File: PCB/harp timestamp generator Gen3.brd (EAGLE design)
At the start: 124.5 x 80.4 mm, 140 parts, among them IC1 MCP73831T-2ATI/OT, IC10 SN74LVC1G125DBVT, IC11 TLV70033DDCR, IC12 SI8621BC-B-IS, IC13 SI8621BC-B-IS, IC14 SI8621BC-B-IS, IC15 SI8621BC-B-IS, IC16 SI8621BC-B-IS, IC17 SI8621BC-B-IS, IC18 SN74LVC1G125DBVT, IC19 SN74LVC1G125DBVT, IC2 USBLC6-2SC6, IC3 FT232RL, IC4 ICL7673CBAZA-T, IC5 TLV70033DDCR, IC6 ATXMEGA16A4U-AU, IC7 M74VHC1GT126DF1G, IC8 M74VHC1GT126DF1G, IC9 M74VHC1GT126DF1G, Q1 RTU002P02T106, Q2 BC817-40W, Q3 BC817-40LT1SMD, Q4 DMG1012UW, Q5 DMP2035U-7, T1 BC850, T10 BC850, T2 BC850, T3 BC850, T4 BC850, T5 BC850, T6 BC850, T7 BC850, T8 BC850, T9 BC850, X1 B2B-PH-K-S(LF)(SN)

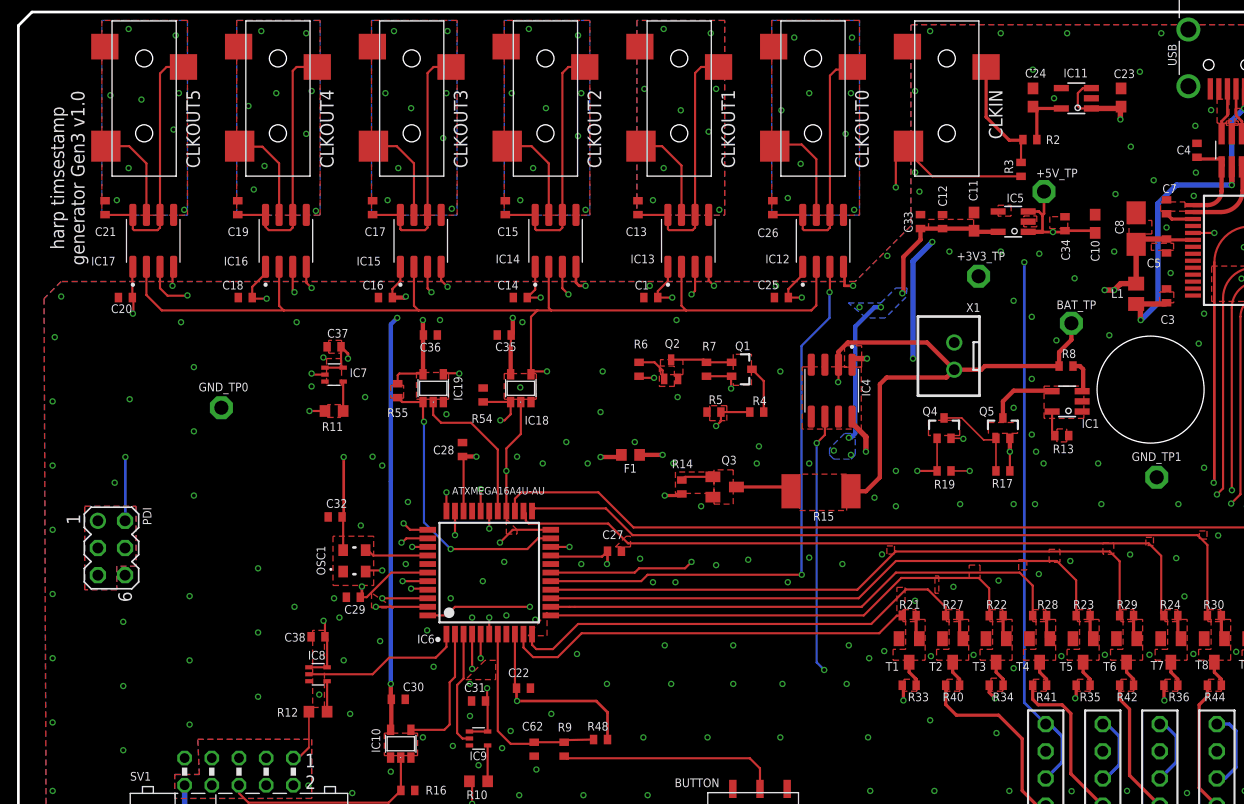
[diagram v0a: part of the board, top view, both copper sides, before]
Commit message: Added an extra 100uF capacitor to +5_USB.
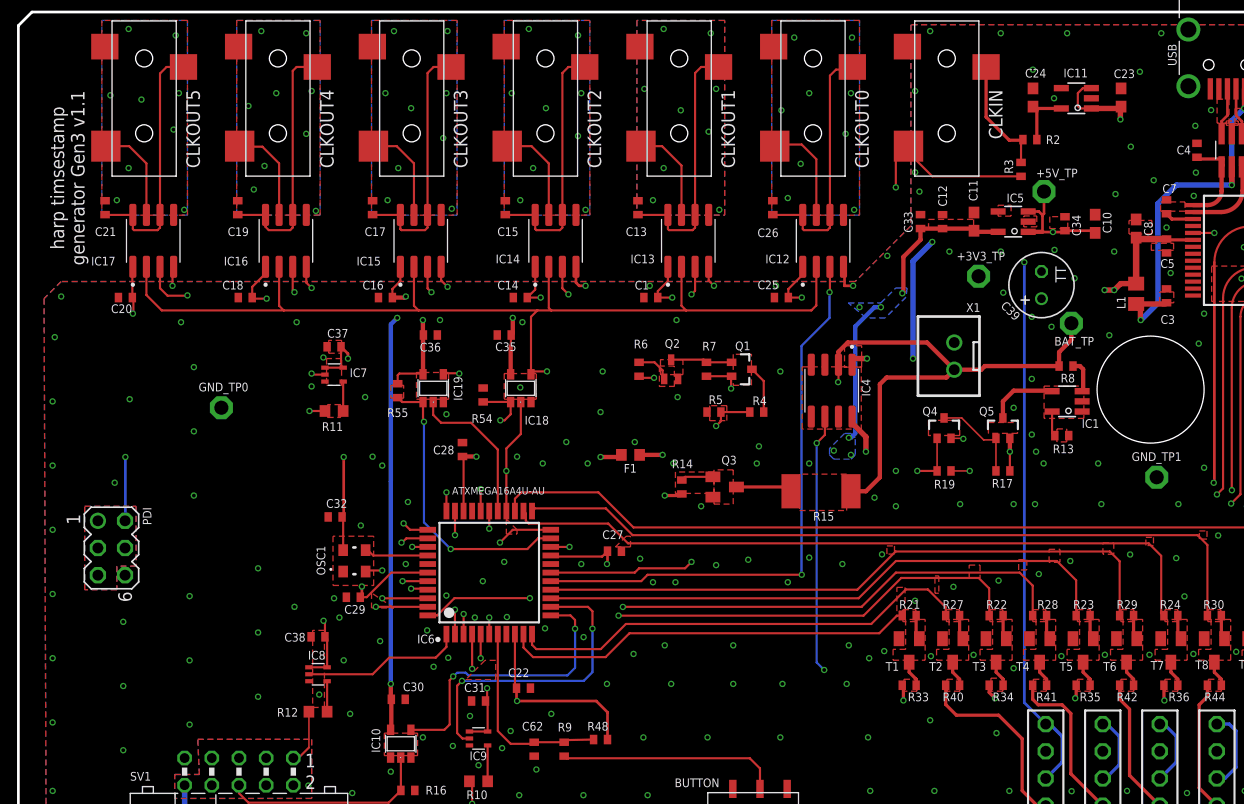
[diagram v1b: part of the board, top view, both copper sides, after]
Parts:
- added C39: 100u 25V, rcl:TT2D6
- C8: device rcl:A/3216-18W -> rcl:C0603
- turned C8 to 90 degrees
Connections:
- net +5_USB: now also C39.+, C8.1; no longer C8.+
- net GND: now also C39.-, C8.2; no longer C8.-
- net LED_CLK_1: now also IC6.3, R22.1; no longer IC6.11, R27.1
- net LED_CLK_2: now also IC6.14, R23.1; no longer IC6.12, R22.1
- net LED_CLK_3: now also IC6.11, R27.1; no longer IC6.13, R28.1
- net LED_CLK_4: now also IC6.2, R28.1; no longer IC6.14, R23.1
- net UC_RX: now also IC6.12; no longer IC6.2
- net UC_TX: now also IC6.13; no longer IC6.3
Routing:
- net UC_TX: track 10.9 -> 28.7 mm, vias 0 -> 2
- net UC_RX: track 12.5 -> 27.3 mm, vias 0 -> 2
- net LED_CLK_1: track 43.6 -> 55.9 mm, vias 0 -> 2
- net LED_CLK_2: track 45.4 -> 54.6 mm
- net LED_CLK_4: track 54.6 -> 61.4 mm, vias 0 -> 2
- net LED_CLK_3: track 49.7 -> 43.6 mm
- net +5_USB: track 56.1 -> 56.8 mm
- net +3V3: track 353.8 -> 354.4 mm
- net GND: vias 226 -> 227
- added copper zone on layer 2, net +5_USB
- removed copper zone on layer 1, net N$82
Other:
- board text added: "harp timsestamp generator Gen3 v1.1"
- board text removed: "harp timsestamp generator Gen3 v1.0"

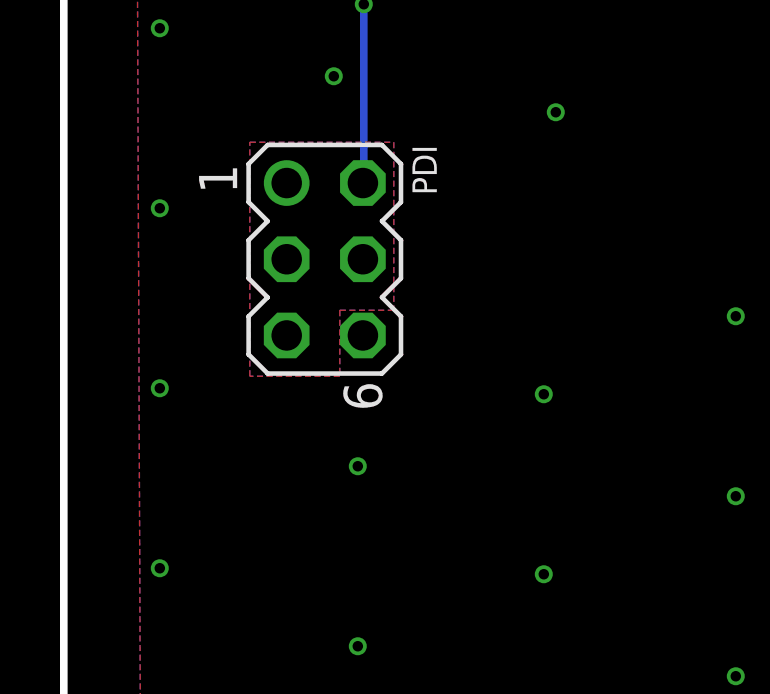
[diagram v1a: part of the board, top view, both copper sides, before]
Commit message: Added proper filtering to RESET line.
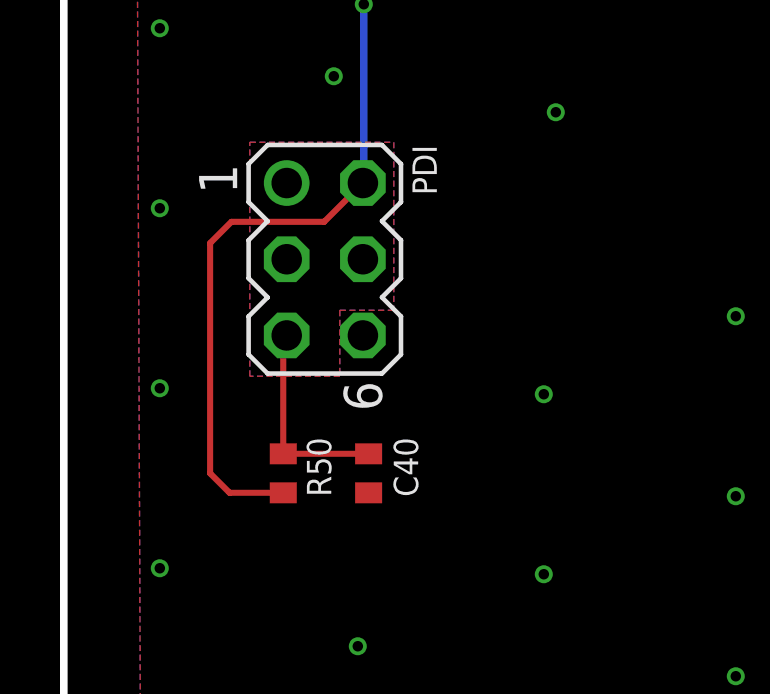
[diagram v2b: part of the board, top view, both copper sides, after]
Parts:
- added C40: 330pF, rcl:C0402
- added R50: 10k, rcl:R0402
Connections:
- net GND: now also C40.2
- net PDI-CLK: now also C40.1, R50.1
- net VDD: now also R50.2
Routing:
- net VDD: track 146.2 -> 162.5 mm
- net PDI-CLK: track 32.2 -> 39.1 mm
- net GND: vias 227 -> 226

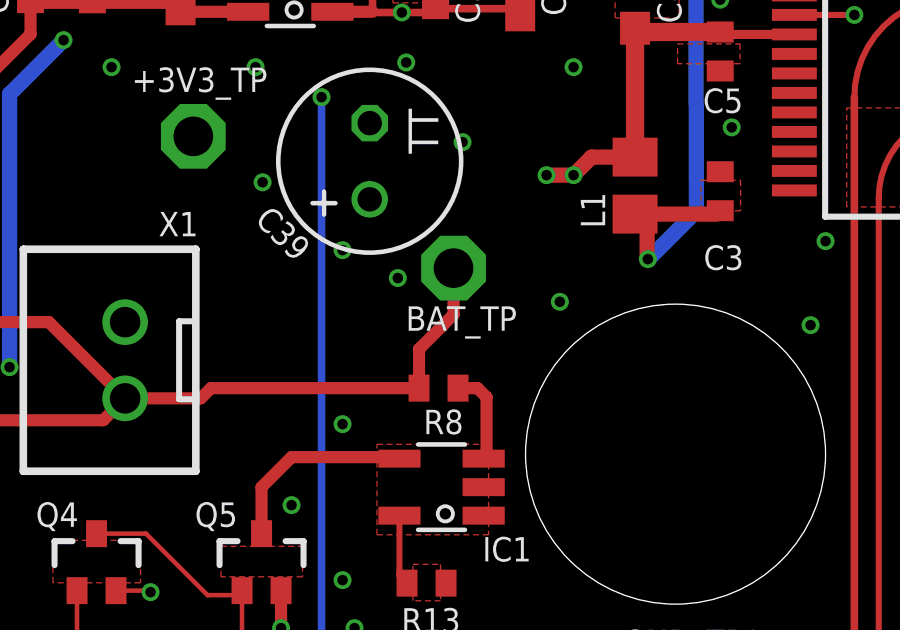
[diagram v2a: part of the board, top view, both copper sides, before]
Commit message: Corrected the discharge circuit.
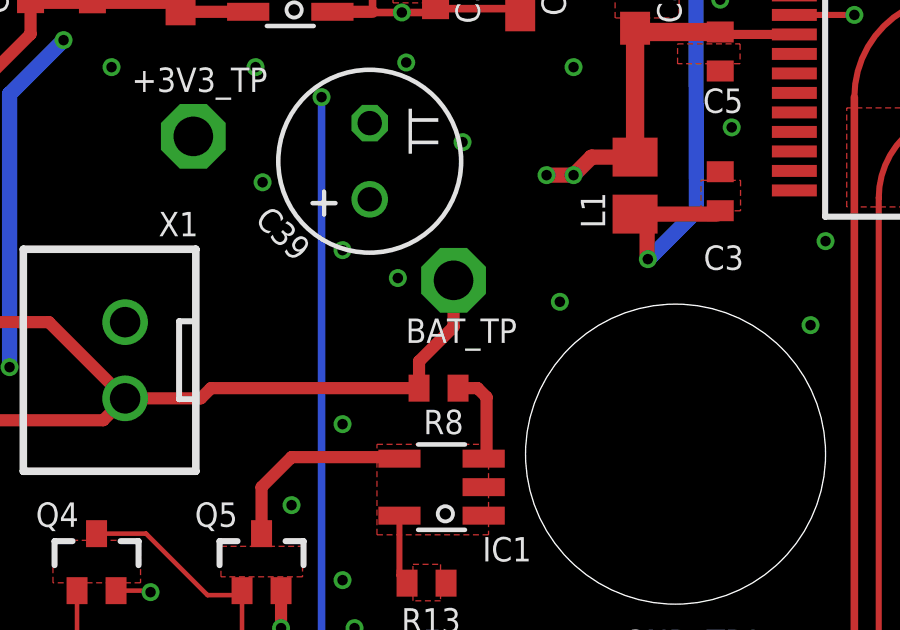
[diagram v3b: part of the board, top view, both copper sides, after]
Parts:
- R14: value 10k -> 1k
- moved BAT_TP 0.41 mm to (98.4, 50.9)
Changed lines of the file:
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@@
 <attribute name="DIGKEYPN" value="ATXMEGA16A4U-AU-ND" x="44" y="28" size="1.778" layer="27" rot="R90" display="off"/>
 <attribute name="MPN" value="ATXMEGA16A4U-AU" x="44" y="28" size="1.778" layer="27" rot="R90" display="off"/>
-<attribute name="NAME" x="38.9" y="22.2" size="0.8128" layer="21" font="vector" ratio="15" rot="R180"/>
 <attribute name="NAME" x="38.2" y="36" size="0.8128" layer="51" font="vector" ratio="15" rot="R180" display="off"/>
+<attribute name="NAME" x="38.9" y="22.2" size="0.8128" layer="21" font="vector" ratio="15" rot="R180"/>
 <attribute name="VALUE" x="49.2" y="36" size="0.7" layer="21" ratio="5" rot="R180"/>
 </element>
@@
 <attribute name="VALUE" x="66.205" y="46.365" size="1.27" layer="27" rot="R90"/>
 </element>
-<element name="BAT_TP" library="testpad" library_urn="urn:adsk.eagle:library:385" package="P1-13" package3d_urn="urn:adsk.eagle:package:27946/1" value="TPPAD1-13" x="98.4" y="51.3" smashed="yes" rot="R180">
-<attribute name="DIGKEYPN" value="" x="98.4" y="51.3" size="1.778" layer="27" rot="R180" display="off"/>
-<attribute name="MPN" value="n.a." x="98.4" y="51.3" size="1.778" layer="27" rot="R180" display="off"/>
-<attribute name="NAME" x="100.5128" y="50.0264" size="0.8128" layer="25" font="vector" ratio="15" rot="R180"/>
-<attribute name="POPULARITY" value="12" x="98.4" y="51.3" size="1.778" layer="27" rot="R180" display="off"/>
-<attribute name="TP_SIGNAL_NAME" value="" x="98.4" y="51.3" size="1.778" layer="27" rot="R180" display="off"/>
-<attribute name="VALUE" x="98.4" y="51.3" size="0.0254" layer="27" rot="R180"/>
+<element name="BAT_TP" library="testpad" library_urn="urn:adsk.eagle:library:385" package="P1-13" package3d_urn="urn:adsk.eagle:package:27946/1" value="TPPAD1-13" x="98.4" y="50.8936" smashed="yes" rot="R180">
+<attribute name="DIGKEYPN" value="" x="98.4" y="50.8936" size="1.778" layer="27" rot="R180" display="off"/>
+<attribute name="MPN" value="n.a." x="98.4" y="50.8936" size="1.778" layer="27" rot="R180" display="off"/>
+<attribute name="NAME" x="100.5128" y="49.62" size="0.8128" layer="25" font="vector" ratio="15" rot="R180"/>
+<attribute name="POPULARITY" value="12" x="98.4" y="50.8936" size="1.778" layer="27" rot="R180" display="off"/>
+<attribute name="TP_SIGNAL_NAME" value="" x="98.4" y="50.8936" size="1.778" layer="27" rot="R180" display="off"/>
+<attribute name="VALUE" x="98.4" y="50.8936" size="0.0254" layer="27" rot="R180"/>
 </element>
 <element name="R8" library="rcl" package="R0402" value="0" x="97.9" y="47.3" smashed="yes" rot="R180">
@@
 <attribute name="VALUE" x="62.825" y="37.905" size="1.27" layer="27" rot="R270"/>
 </element>
-<element name="R14" library="rcl" package="R0402" value="10k" x="62" y="36" smashed="yes" rot="R90">
+<element name="R14" library="rcl" package="R0402" value="1k" x="62" y="36" smashed="yes" rot="R90">
 <attribute name="DIGKEYPN" value="541-3959-1-ND" x="62" y="36" size="1.778" layer="27" rot="R90" display="off"/>
 <attribute name="MPN" value="CRCW040210K0FKEDC" x="62" y="36" size="1.778" layer="27" rot="R90" display="off"/>
@@
 <wire x1="80.5" y1="36.9" x2="80.5" y2="45.6" width="0.4064" layer="1"/>
 <wire x1="80.5" y1="45.6" x2="81.13" y2="46.23" width="0.4064" layer="1"/>
-<wire x1="98.4" y1="51.3" x2="98.4" y2="49.75" width="0.4064" layer="1"/>
-<wire x1="98.4" y1="49.75" x2="97.25" y2="48.6" width="0.4064" layer="1"/>
-<wire x1="97.25" y1="47.3" x2="97.25" y2="48.6" width="0.4064" layer="1"/>
+<wire x1="98.4" y1="50.8936" x2="98.4" y2="49.3436" width="0.4064" layer="1"/>
+<wire x1="98.4" y1="49.3436" x2="97.25" y2="48.1936" width="0.4064" layer="1"/>
+<wire x1="97.25" y1="47.3" x2="97.25" y2="48.1936" width="0.4064" layer="1"/>
 <wire x1="76.635" y1="47.425" x2="76.635" y2="45.835" width="0.2032" layer="1"/>
 <wire x1="76.635" y1="45.835" x2="76.6" y2="45.8" width="0.2032" layer="1"/>

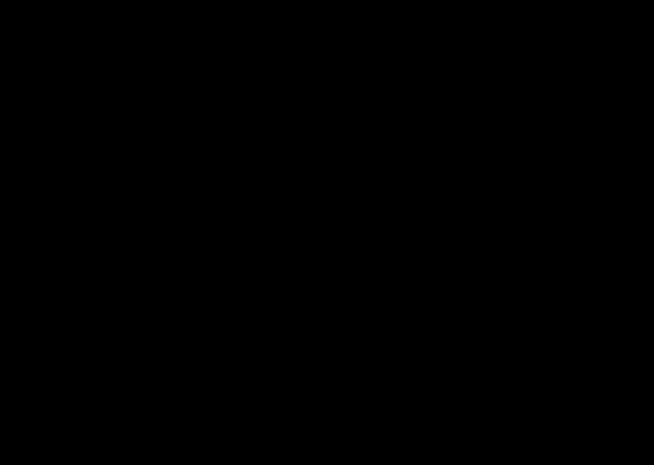
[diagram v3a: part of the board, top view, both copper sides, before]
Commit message: Decreased discharge current by ~60 mA to ~175 mA in average.
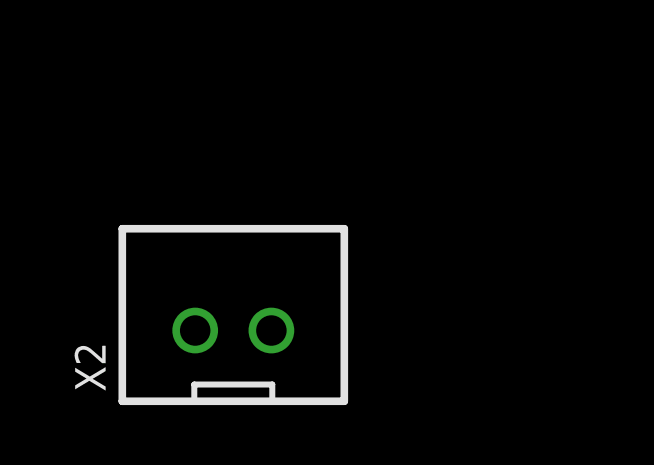
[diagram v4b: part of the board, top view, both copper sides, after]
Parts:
- added X2: B2B-PH-K-S(LF)(SN), harp timestamp generator:JST-XH-02-PACKAGE-ROUND-PAD
- R15: value 15R -> 20R
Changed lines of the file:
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@@
 <attribute name="DIGKEYPN" value="ATXMEGA16A4U-AU-ND" x="44" y="28" size="1.778" layer="27" rot="R90" display="off"/>
 <attribute name="MPN" value="ATXMEGA16A4U-AU" x="44" y="28" size="1.778" layer="27" rot="R90" display="off"/>
+<attribute name="NAME" x="38.9" y="22.2" size="0.8128" layer="21" font="vector" ratio="15" rot="R180"/>
 <attribute name="NAME" x="38.2" y="36" size="0.8128" layer="51" font="vector" ratio="15" rot="R180" display="off"/>
-<attribute name="NAME" x="38.9" y="22.2" size="0.8128" layer="21" font="vector" ratio="15" rot="R180"/>
 <attribute name="VALUE" x="49.2" y="36" size="0.7" layer="21" ratio="5" rot="R180"/>
 </element>
@@
 <attribute name="VALUE" x="63.905" y="35.365" size="1.27" layer="27" rot="R90"/>
 </element>
-<element name="R15" library="rcl" package="R2512" value="15R" x="75" y="35.6" smashed="yes" rot="R180">
+<element name="R15" library="rcl" package="R2512" value="20R" x="75" y="35.6" smashed="yes" rot="R180">
 <attribute name="DIGKEYPN" value="541-2662-1-ND" x="75" y="35.6" size="1.778" layer="27" rot="R180" display="off"/>
 <attribute name="MPN" value="RCP2512W25R0GEB" x="75" y="35.6" size="1.778" layer="27" rot="R180" display="off"/>
@@
 <attribute name="VALUE" x="8.255" y="23.7998" size="1.27" layer="27" rot="R270"/>
 </element>
+<element name="X2" library="harp timestamp generator" package="JST-XH-02-PACKAGE-ROUND-PAD" value="B2B-PH-K-S(LF)(SN)" x="-60.96" y="-10.9728" smashed="yes">
+<attribute name="DIGKEYPN" value="455-1704-ND" x="-60.96" y="-10.9728" size="1.778" layer="27" display="off"/>
+<attribute name="MPN" value="B2B-PH-K-S(LF)(SN)" x="-60.96" y="-10.9728" size="1.778" layer="27" display="off"/>
+<attribute name="NAME" x="-65.215" y="-13.0128" size="1.016" layer="25" ratio="10" rot="R90"/>
+<attribute name="VALUE" x="-64.2625" y="-7.0803" size="1.016" layer="27" ratio="10"/>
+</element>
 </elements>
